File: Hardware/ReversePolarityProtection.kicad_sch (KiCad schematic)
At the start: 14 parts, among them CON1 VIN, CON2 GND, CON3 VOUT, CON4 GND, J1 Screw_Terminal_01x02, Q1 SUM40N10-30-E3, U1 LM5050-1

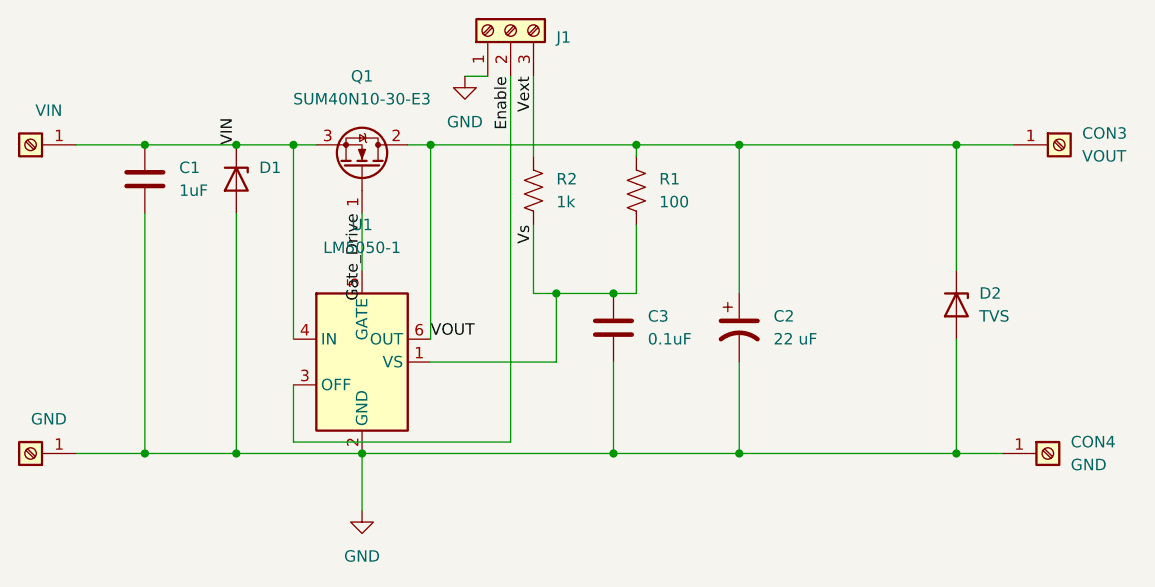
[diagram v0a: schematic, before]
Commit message: Fix missing D2
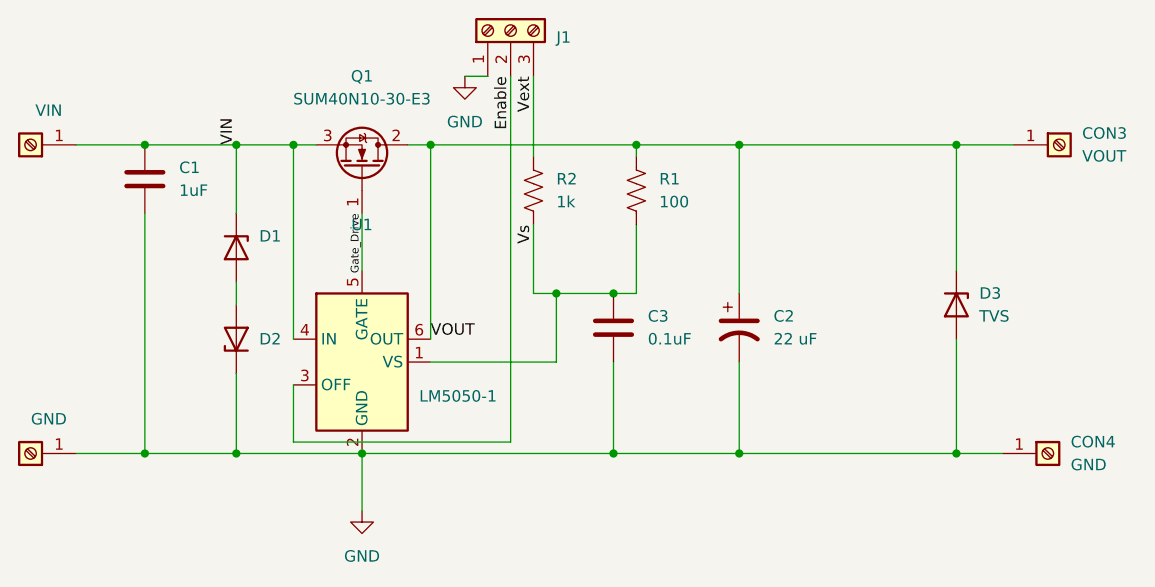
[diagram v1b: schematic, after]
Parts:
- added D2: SS16T3G, Diode_SMD:D_SMA-SMB_Universal_Handsoldering, symbol Device:D_Zener
- renumbered D2 to D3
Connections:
- net GND: now also D2.1 (K); no longer D1.2 (A)
- new net: D1.2 (A), D2.2 (A)
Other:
- moved on the sheet: D1
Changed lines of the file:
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@@
+	)
+	(junction
+		(at 63.5 35.56)
+		(diameter 0)
+		(color 0 0 0 0)
 	)
 	(junction
@@
 	)
 	(junction
-		(at 63.5 35.56)
-		(diameter 0.9144)
-		(color 0 0 0 0)
-	)
-	(junction
 		(at 143.51 35.56)
 		(diameter 0.9144)
@@
 	(wire
 		(pts
+			(xy 63.5 53.34) (xy 63.5 50.8)
+		)
+		(stroke
+			(width 0)
+			(type solid)
+		)
+	)
+	(wire
+		(pts
 			(xy 85.09 59.69) (xy 99.06 59.69)
 		)
@@
 	(wire
 		(pts
-			(xy 63.5 69.85) (xy 63.5 43.18)
+			(xy 63.5 69.85) (xy 63.5 60.96)
 		)
 		(stroke
@@
 	(wire
 		(pts
+			(xy 107.95 35.56) (xy 119.38 35.56)
+		)
+		(stroke
+			(width 0)
+			(type solid)
+		)
+	)
+	(wire
+		(pts
+			(xy 119.38 35.56) (xy 119.38 52.07)
+		)
+		(stroke
+			(width 0)
+			(type solid)
+		)
+	)
+	(wire
+		(pts
+			(xy 105.41 52.07) (xy 107.95 52.07)
+		)
+		(stroke
+			(width 0)
+			(type solid)
+		)
+	)
+	(wire
+		(pts
+			(xy 107.95 52.07) (xy 107.95 44.45)
+		)
+		(stroke
+			(width 0)
+			(type solid)
+		)
+	)
+	(wire
+		(pts
+			(xy 143.51 35.56) (xy 119.38 35.56)
+		)
+		(stroke
+			(width 0)
+			(type solid)
+		)
+	)
+	(wire
+		(pts
+			(xy 143.51 49.53) (xy 143.51 35.56)
+		)
+		(stroke
+			(width 0)
+			(type solid)
+		)
+	)
+	(wire
+		(pts
+			(xy 69.85 35.56) (xy 69.85 57.15)
+		)
+		(stroke
+			(width 0)
+			(type solid)
+		)
+	)
+	(wire
+		(pts
+			(xy 72.39 35.56) (xy 69.85 35.56)
+		)
+		(stroke
+			(width 0)
+			(type solid)
+		)
+	)
+	(wire
+		(pts
+			(xy 45.72 35.56) (xy 53.34 35.56)
+		)
+		(stroke
+			(width 0)
+			(type solid)
+		)
+	)
+	(wire
+		(pts
 			(xy 63.5 35.56) (xy 69.85 35.56)
 		)
@@
 	(wire
 		(pts
-			(xy 107.95 35.56) (xy 119.38 35.56)
-		)
-		(stroke
-			(width 0)
-			(type solid)
-		)
-	)
-	(wire
-		(pts
-			(xy 119.38 35.56) (xy 119.38 52.07)
-		)
-		(stroke
-			(width 0)
-			(type solid)
-		)
-	)
-	(wire
-		(pts
-			(xy 105.41 52.07) (xy 107.95 52.07)
-		)
-		(stroke
-			(width 0)
-			(type solid)
-		)
-	)
-	(wire
-		(pts
-			(xy 107.95 52.07) (xy 107.95 44.45)
-		)
-		(stroke
-			(width 0)
-			(type solid)
-		)
-	)
-	(wire
-		(pts
-			(xy 143.51 35.56) (xy 119.38 35.56)
-		)
-		(stroke
-			(width 0)
-			(type solid)
-		)
-	)
-	(wire
-		(pts
-			(xy 143.51 49.53) (xy 143.51 35.56)
-		)
-		(stroke
-			(width 0)
-			(type solid)
-		)
-	)
-	(wire
-		(pts
-			(xy 69.85 35.56) (xy 69.85 57.15)
-		)
-		(stroke
-			(width 0)
-			(type solid)
-		)
-	)
-	(wire
-		(pts
-			(xy 72.39 35.56) (xy 69.85 35.56)
-		)
-		(stroke
-			(width 0)
-			(type solid)
-		)
-	)
-	(wire
-		(pts
-			(xy 45.72 35.56) (xy 53.34 35.56)
-		)
-		(stroke
-			(width 0)
-			(type solid)
-		)
-	)
-	(wire
-		(pts
 			(xy 119.38 59.69) (xy 119.38 69.85)
 		)
@@
 			(width 0)
 			(type solid)
+		)
+	)
+	(wire
+		(pts
+			(xy 63.5 43.18) (xy 63.5 35.56)
+		)
+		(stroke
+			(width 0)
+			(type default)
 		)
 	)
@@
 		(effects
 			(font
-				(size 1.27 1.27)
+				(size 0.87 0.87)
 			)
 			(justify right bottom)
@@
 		)
 		(instances
-			(project "Reverse Polarity Protection"
+			(project "ReversePolarityProtection"
 				(path "/8ebbf97a-67d0-41db-be0c-70330c9ca5ce"
 					(reference "CON3")
@@
 		)
 		(instances
-			(project "Reverse Polarity Protection"
+			(project "ReversePolarityProtection"
 				(path "/8ebbf97a-67d0-41db-be0c-70330c9ca5ce"
 					(reference "C1")
@@
 		)
 		(instances
-			(project "Reverse Polarity Protection"
+			(project "ReversePolarityProtection"
 				(path "/8ebbf97a-67d0-41db-be0c-70330c9ca5ce"
 					(reference "CON2")
@@
 		)
 		(instances
-			(project "Reverse Polarity Protection"
+			(project "ReversePolarityProtection"
 				(path "/8ebbf97a-67d0-41db-be0c-70330c9ca5ce"
 					(reference "CON1")
@@
 		)
 		(instances
-			(project "Reverse Polarity Protection"
+			(project "ReversePolarityProtection"
 				(path "/8ebbf97a-67d0-41db-be0c-70330c9ca5ce"
 					(reference "CON4")
@@
 		)
 		(instances
-			(project "Reverse Polarity Protection"
+			(project "ReversePolarityProtection"
 				(path "/8ebbf97a-67d0-41db-be0c-70330c9ca5ce"
 					(reference "C2")
@@
 		(on_board yes)
 		(dnp no)
-		(fields_autoplaced yes)
 		(property "Reference" "U1"
 			(at 77.47 44.45 0)
@@
 		)
 		(property "Value" "LM5050-1"
-			(at 77.47 46.99 0)
+			(at 88.138 63.5 0)
 			(effects
 				(font
@@
 		)
 		(instances
-			(project "Reverse Polarity Protection"
+			(project "ReversePolarityProtection"
 				(path "/8ebbf97a-67d0-41db-be0c-70330c9ca5ce"
 					(reference "U1")
@@
 		(dnp no)
 		(fields_autoplaced yes)
-		(property "Reference" "D2"
+		(property "Reference" "D3"
 			(at 146.05 52.0699 90)
 			(effects
@@
 		)
 		(instances
-			(project "Reverse Polarity Protection"
+			(project "ReversePolarityProtection"
 				(path "/8ebbf97a-67d0-41db-be0c-70330c9ca5ce"
-					(reference "D2")
+					(reference "D3")
 					(unit 1)
 				)
@@
 		)
 		(instances
-			(project "Reverse Polarity Protection"
+			(project "ReversePolarityProtection"
 				(path "/8ebbf97a-67d0-41db-be0c-70330c9ca5ce"
 					(reference "R1")
@@
 		)
 		(instances
-			(project "Reverse Polarity Protection"
+			(project "ReversePolarityProtection"
 				(path "/8ebbf97a-67d0-41db-be0c-70330c9ca5ce"
 					(reference "#PWR0101")
@@
 		)
 		(instances
-			(project "Reverse Polarity Protection"
+			(project "ReversePolarityProtection"
 				(path "/8ebbf97a-67d0-41db-be0c-70330c9ca5ce"
 					(reference "R2")
@@
 		)
 		(instances
-			(project "Reverse Polarity Protection"
+			(project "ReversePolarityProtection"
 				(path "/8ebbf97a-67d0-41db-be0c-70330c9ca5ce"
 					(reference "J1")
+					(unit 1)
+				)
+			)
+		)
+	)
+	(symbol
+		(lib_id "Device:D_Zener")
+		(at 63.5 57.15 90)
+		(unit 1)
+		(exclude_from_sim no)
+		(in_bom yes)
+		(on_board yes)
+		(dnp no)
+		(fields_autoplaced yes)
+		(property "Reference" "D2"
+			(at 66.04 57.1499 90)
+			(effects
+				(font
+					(size 1.27 1.27)
+				)
+				(justify right)
+			)
+		)
+		(property "Value" "SS16T3G"
+			(at 60.96 55.8801 90)
+			(effects
+				(font
+					(size 1.27 1.27)
+				)
+				(justify left)
+				(hide yes)
+			)
+		)
+		(property "Footprint" "Diode_SMD:D_SMA-SMB_Universal_Handsoldering"
+			(at 63.5 57.15 0)
+			(effects
+				(font
+					(size 1.27 1.27)
+				)
+				(hide yes)
+			)
+		)
+		(property "Datasheet" "~"
+			(at 63.5 57.15 0)
+			(effects
+				(font
+					(size 1.27 1.27)
+				)
+				(hide yes)
+			)
+		)
+		(property "Description" ""
+			(at 63.5 57.15 0)
+			(effects
+				(font
+					(size 1.27 1.27)
+				)
+				(hide yes)
+			)
+		)
+		(pin "1"
+		)
+		(pin "2"
+		)
+		(instances
+			(project "ReversePolarityProtection"
+				(path "/8ebbf97a-67d0-41db-be0c-70330c9ca5ce"
+					(reference "D2")
 					(unit 1)
 				)
@@
 		)
 		(instances
-			(project "Reverse Polarity Protection"
+			(project "ReversePolarityProtection"
 				(path "/8ebbf97a-67d0-41db-be0c-70330c9ca5ce"
 					(reference "#PWR0102")
@@
 		)
 		(instances
-			(project "Reverse Polarity Protection"
+			(project "ReversePolarityProtection"
 				(path "/8ebbf97a-67d0-41db-be0c-70330c9ca5ce"
 					(reference "Q1")
@@
 		)
 		(instances
-			(project "Reverse Polarity Protection"
+			(project "ReversePolarityProtection"
 				(path "/8ebbf97a-67d0-41db-be0c-70330c9ca5ce"
 					(reference "C3")
@@
 	(symbol
 		(lib_id "Device:D_Zener")
-		(at 63.5 39.37 270)
+		(at 63.5 46.99 270)
 		(unit 1)
 		(exclude_from_sim no)
@@
 		(fields_autoplaced yes)
 		(property "Reference" "D1"
-			(at 66.04 38.0999 90)
+			(at 66.04 45.7199 90)
 			(effects
 				(font
@@
 		)
 		(property "Value" "SS16T3G"
-			(at 66.04 40.6399 90)
+			(at 66.04 48.2599 90)
 			(effects
 				(font
@@
 		)
 		(property "Footprint" "Diode_SMD:D_SMA-SMB_Universal_Handsoldering"
-			(at 63.5 39.37 0)
+			(at 63.5 46.99 0)
 			(effects
 				(font
@@
 		)
 		(property "Datasheet" "~"
-			(at 63.5 39.37 0)
+			(at 63.5 46.99 0)
 			(effects
 				(font
@@
 		)
 		(property "Description" ""
-			(at 63.5 39.37 0)
+			(at 63.5 46.99 0)
 			(effects
 				(font
@@
 		)
 		(instances
-			(project "Reverse Polarity Protection"
+			(project "ReversePolarityProtection"
 				(path "/8ebbf97a-67d0-41db-be0c-70330c9ca5ce"
 					(reference "D1")
